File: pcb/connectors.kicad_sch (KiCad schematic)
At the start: 7 parts, among them J1 USB_C_Receptacle_USB2.0, J5 Conn_01x04, U6 USBLC6-2SC6

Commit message: Schematic done, starting PCB design
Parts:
- removed J5: Conn_01x04, Connector_PinSocket_2.54mm:PinSocket_1x04_P2.54mm_Horizontal, symbol Connector_Generic:Conn_01x04
- removed R1, R2, R3, R4: 10.2k, Resistor_SMD:R_0603_1608Metric, symbol Device:R
- added R11 (x4): 10k, Resistor_SMD:R_0603_1608Metric_Pad0.98x0.95mm_HandSolder, symbol Device:R
- added TP1, TP2: TestPoint, TestPoint:TestPoint_Pad_D2.0mm, symbol Connector:TestPoint
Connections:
- net CC1: now also R11.1, R11.1
- net CC2: now also R11.1, R11.1
- net GND: now also R11.2, R11.2, R11.2, R11.2; no longer J1.S1 (SHIELD)
- net SWCLK: now also TP2.1
- net SWDIO: now also TP1.1
- no-connect marks 2 -> 3
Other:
- note added: "Ground loop moment"
- note added: "Solder wires to test points in the unlikely event that you need to debug or enter rescue DP"
- note added: "Try make these 10k resistors toleranced +-5% or lower"
- moved on the sheet: J1, U6

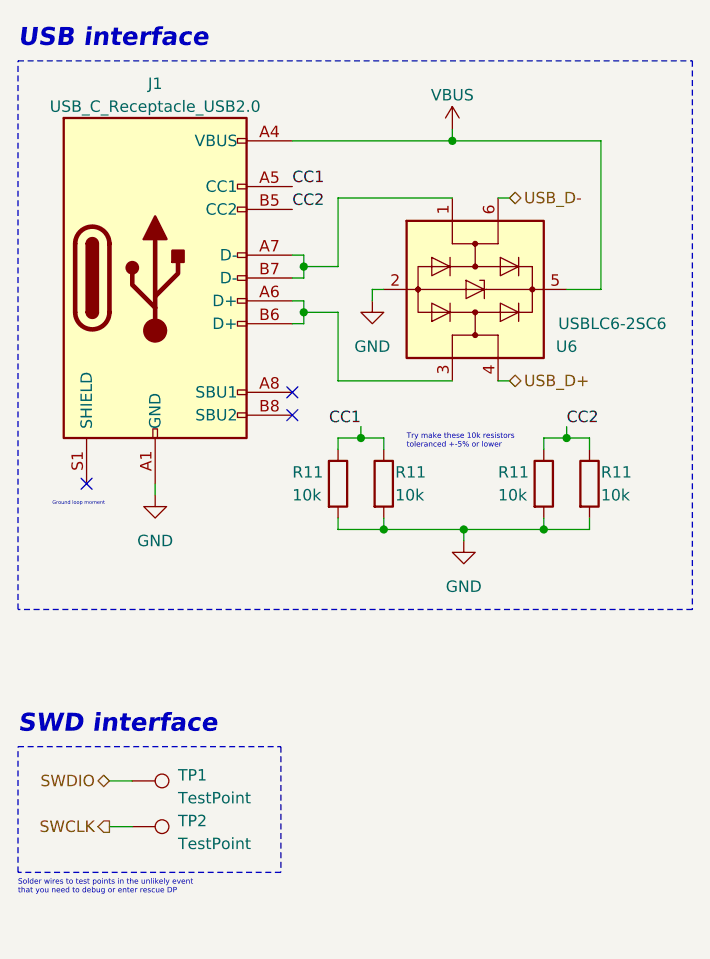
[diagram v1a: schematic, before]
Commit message: Rerouted a lot of stuff
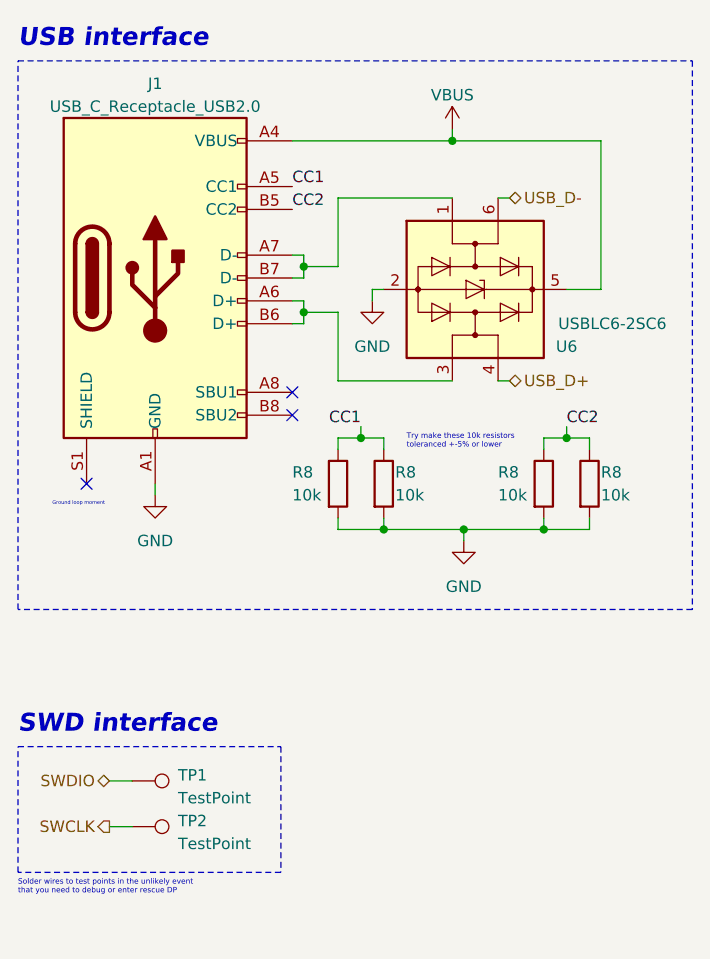
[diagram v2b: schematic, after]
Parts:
- removed R11 (x4): 10k, Resistor_SMD:R_0603_1608Metric_Pad0.98x0.95mm_HandSolder, symbol Device:R
- added R8 (x4): 10k, Resistor_SMD:R_0402_1005Metric, symbol Device:R
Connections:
- net CC1: now also R8.1, R8.1
- net CC2: now also R8.1, R8.1
- net GND: now also R8.2, R8.2, R8.2, R8.2
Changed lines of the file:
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@@
+    )
+  )
+  (symbol (lib_id "Device:R") (at 60.96 72.39 0) (unit 1)
+    (in_bom yes) (on_board yes) (dnp no)
+    (property "Reference" "R8" (at 55.88 71.12 0)
+      (effects (font (size 1.27 1.27)) (justify left))
+    )
+    (property "Value" "10k" (at 55.88 73.66 0)
+      (effects (font (size 1.27 1.27)) (justify left))
+    )
+    (property "Footprint" "Resistor_SMD:R_0402_1005Metric" (at 59.182 72.39 90)
+      (effects (font (size 1.27 1.27)) hide)
+    )
+    (property "Datasheet" "~" (at 60.96 72.39 0)
+      (effects (font (size 1.27 1.27)) hide)
+    )
+    (pin "1")
+    (pin "2")
+    (instances
+      (project "keyboard"
+        (path "/fc529d87-72d0-4c92-b352-ddcf4c6f7199/1c8ac5bd-b3bc-4835-a71b-e635010cd696"
+          (reference "R8") (unit 1)
+        )
+        (path "/fc529d87-72d0-4c92-b352-ddcf4c6f7199/953c467c-8c0d-4158-80e9-7f51ef1515ee"
+          (reference "R7") (unit 1)
+        )
+      )
+    )
+  )
+  (symbol (lib_id "Connector:TestPoint") (at 38.1 110.49 270) (unit 1)
+    (in_bom yes) (on_board yes) (dnp no) (fields_autoplaced)
+    (property "Reference" "TP2" (at 43.18 109.855 90)
+      (effects (font (size 1.27 1.27)) (justify left))
+    )
+    (property "Value" "TestPoint" (at 43.18 112.395 90)
+      (effects (font (size 1.27 1.27)) (justify left))
+    )
+    (property "Footprint" "TestPoint:TestPoint_Pad_D2.0mm" (at 38.1 115.57 0)
+      (effects (font (size 1.27 1.27)) hide)
+    )
+    (property "Datasheet" "~" (at 38.1 115.57 0)
+      (effects (font (size 1.27 1.27)) hide)
+    )
+    (pin "1")
+    (instances
+      (project "keyboard"
+        (path "/fc529d87-72d0-4c92-b352-ddcf4c6f7199/953c467c-8c0d-4158-80e9-7f51ef1515ee"
+          (reference "TP2") (unit 1)
+        )
+      )
     )
   )
   (symbol (lib_id "Device:R") (at 83.82 72.39 0) (unit 1)
     (in_bom yes) (on_board yes) (dnp no)
-    (property "Reference" "R11" (at 78.74 71.12 0)
+    (property "Reference" "R8" (at 78.74 71.12 0)
       (effects (font (size 1.27 1.27)) (justify left))
     )
@@
       (effects (font (size 1.27 1.27)) (justify left))
     )
-    (property "Footprint" "Resistor_SMD:R_0603_1608Metric_Pad0.98x0.95mm_HandSolder" (at 82.042 72.39 90)
+    (property "Footprint" "Resistor_SMD:R_0402_1005Metric" (at 82.042 72.39 90)
       (effects (font (size 1.27 1.27)) hide)
     )
@@
       (project "keyboard"
         (path "/fc529d87-72d0-4c92-b352-ddcf4c6f7199/1c8ac5bd-b3bc-4835-a71b-e635010cd696"
-          (reference "R11") (unit 1)
-        )
-        (path "/fc529d87-72d0-4c92-b352-ddcf4c6f7199/953c467c-8c0d-4158-80e9-7f51ef1515ee"
-          (reference "R6") (unit 1)
-        )
-      )
-    )
-  )
-  (symbol (lib_id "Device:R") (at 66.04 72.39 0) (unit 1)
-    (in_bom yes) (on_board yes) (dnp no)
-    (property "Reference" "R11" (at 67.31 71.12 0)
-      (effects (font (size 1.27 1.27)) (justify left))
-    )
-    (property "Value" "10k" (at 67.31 73.66 0)
-      (effects (font (size 1.27 1.27)) (justify left))
-    )
-    (property "Footprint" "Resistor_SMD:R_0603_1608Metric_Pad0.98x0.95mm_HandSolder" (at 64.262 72.39 90)
-      (effects (font (size 1.27 1.27)) hide)
-    )
-    (property "Datasheet" "~" (at 66.04 72.39 0)
-      (effects (font (size 1.27 1.27)) hide)
-    )
-    (pin "1")
-    (pin "2")
-    (instances
-      (project "keyboard"
-        (path "/fc529d87-72d0-4c92-b352-ddcf4c6f7199/1c8ac5bd-b3bc-4835-a71b-e635010cd696"
-          (reference "R11") (unit 1)
-        )
-        (path "/fc529d87-72d0-4c92-b352-ddcf4c6f7199/953c467c-8c0d-4158-80e9-7f51ef1515ee"
-          (reference "R5") (unit 1)
-        )
-      )
-    )
-  )
-  (symbol (lib_id "Connector:TestPoint") (at 38.1 110.49 270) (unit 1)
-    (in_bom yes) (on_board yes) (dnp no) (fields_autoplaced)
-    (property "Reference" "TP2" (at 43.18 109.855 90)
-      (effects (font (size 1.27 1.27)) (justify left))
-    )
-    (property "Value" "TestPoint" (at 43.18 112.395 90)
-      (effects (font (size 1.27 1.27)) (justify left))
-    )
-    (property "Footprint" "TestPoint:TestPoint_Pad_D2.0mm" (at 38.1 115.57 0)
-      (effects (font (size 1.27 1.27)) hide)
-    )
-    (property "Datasheet" "~" (at 38.1 115.57 0)
-      (effects (font (size 1.27 1.27)) hide)
-    )
-    (pin "1")
-    (instances
-      (project "keyboard"
-        (path "/fc529d87-72d0-4c92-b352-ddcf4c6f7199/953c467c-8c0d-4158-80e9-7f51ef1515ee"
-          (reference "TP2") (unit 1)
+          (reference "R8") (unit 1)
+        )
+        (path "/fc529d87-72d0-4c92-b352-ddcf4c6f7199/953c467c-8c0d-4158-80e9-7f51ef1515ee"
+          (reference "R4") (unit 1)
         )
       )
@@
     )
   )
-  (symbol (lib_id "Device:R") (at 88.9 72.39 0) (unit 1)
-    (in_bom yes) (on_board yes) (dnp no)
-    (property "Reference" "R11" (at 90.17 71.12 0)
-      (effects (font (size 1.27 1.27)) (justify left))
-    )
-    (property "Value" "10k" (at 90.17 73.66 0)
-      (effects (font (size 1.27 1.27)) (justify left))
-    )
-    (property "Footprint" "Resistor_SMD:R_0603_1608Metric_Pad0.98x0.95mm_HandSolder" (at 87.122 72.39 90)
-      (effects (font (size 1.27 1.27)) hide)
-    )
-    (property "Datasheet" "~" (at 88.9 72.39 0)
-      (effects (font (size 1.27 1.27)) hide)
-    )
-    (pin "1")
-    (pin "2")
-    (instances
-      (project "keyboard"
-        (path "/fc529d87-72d0-4c92-b352-ddcf4c6f7199/1c8ac5bd-b3bc-4835-a71b-e635010cd696"
-          (reference "R11") (unit 1)
-        )
-        (path "/fc529d87-72d0-4c92-b352-ddcf4c6f7199/953c467c-8c0d-4158-80e9-7f51ef1515ee"
-          (reference "R7") (unit 1)
+  (symbol (lib_id "Device:R") (at 66.04 72.39 0) (unit 1)
+    (in_bom yes) (on_board yes) (dnp no)
+    (property "Reference" "R8" (at 67.31 71.12 0)
+      (effects (font (size 1.27 1.27)) (justify left))
+    )
+    (property "Value" "10k" (at 67.31 73.66 0)
+      (effects (font (size 1.27 1.27)) (justify left))
+    )
+    (property "Footprint" "Resistor_SMD:R_0402_1005Metric" (at 64.262 72.39 90)
+      (effects (font (size 1.27 1.27)) hide)
+    )
+    (property "Datasheet" "~" (at 66.04 72.39 0)
+      (effects (font (size 1.27 1.27)) hide)
+    )
+    (pin "1")
+    (pin "2")
+    (instances
+      (project "keyboard"
+        (path "/fc529d87-72d0-4c92-b352-ddcf4c6f7199/1c8ac5bd-b3bc-4835-a71b-e635010cd696"
+          (reference "R8") (unit 1)
+        )
+        (path "/fc529d87-72d0-4c92-b352-ddcf4c6f7199/953c467c-8c0d-4158-80e9-7f51ef1515ee"
+          (reference "R6") (unit 1)
         )
       )
@@
     )
   )
-  (symbol (lib_id "Device:R") (at 60.96 72.39 0) (unit 1)
-    (in_bom yes) (on_board yes) (dnp no)
-    (property "Reference" "R11" (at 55.88 71.12 0)
-      (effects (font (size 1.27 1.27)) (justify left))
-    )
-    (property "Value" "10k" (at 55.88 73.66 0)
-      (effects (font (size 1.27 1.27)) (justify left))
-    )
-    (property "Footprint" "Resistor_SMD:R_0603_1608Metric_Pad0.98x0.95mm_HandSolder" (at 59.182 72.39 90)
-      (effects (font (size 1.27 1.27)) hide)
-    )
-    (property "Datasheet" "~" (at 60.96 72.39 0)
-      (effects (font (size 1.27 1.27)) hide)
-    )
-    (pin "1")
-    (pin "2")
-    (instances
-      (project "keyboard"
-        (path "/fc529d87-72d0-4c92-b352-ddcf4c6f7199/1c8ac5bd-b3bc-4835-a71b-e635010cd696"
-          (reference "R11") (unit 1)
-        )
-        (path "/fc529d87-72d0-4c92-b352-ddcf4c6f7199/953c467c-8c0d-4158-80e9-7f51ef1515ee"
-          (reference "R4") (unit 1)
-        )
-      )
+  (symbol (lib_id "Device:R") (at 88.9 72.39 0) (unit 1)
+    (in_bom yes) (on_board yes) (dnp no)
+    (property "Reference" "R8" (at 90.17 71.12 0)
+      (effects (font (size 1.27 1.27)) (justify left))
+    )
+    (property "Value" "10k" (at 90.17 73.66 0)
+      (effects (font (size 1.27 1.27)) (justify left))
+    )
+    (property "Footprint" "Resistor_SMD:R_0402_1005Metric" (at 87.122 72.39 90)
+      (effects (font (size 1.27 1.27)) hide)
+    )
+    (property "Datasheet" "~" (at 88.9 72.39 0)
+      (effects (font (size 1.27 1.27)) hide)
+    )
+    (pin "1")
+    (pin "2")
+    (instances
+      (project "keyboard"
+        (path "/fc529d87-72d0-4c92-b352-ddcf4c6f7199/1c8ac5bd-b3bc-4835-a71b-e635010cd696"
+          (reference "R8") (unit 1)
+        )
+        (path "/fc529d87-72d0-4c92-b352-ddcf4c6f7199/953c467c-8c0d-4158-80e9-7f51ef1515ee"
+          (reference "R5") (unit 1)
+        )
+      )

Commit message: PCB design complete
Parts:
- added TP3: TestPoint, TestPoint:TestPoint_Pad_D2.0mm, symbol Connector:TestPoint
- R8: LCSC (none) -> C25744
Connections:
- net GND: now also TP3.1
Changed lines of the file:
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@@
+    (stroke (width 0) (type default))
+  )
+  (wire (pts (xy 35.56 115.57) (xy 38.1 115.57))
     (stroke (width 0) (type default))
   )
@@
     (fill (type none))
   )
-  (rectangle (start 25.4 101.6) (end 54.61 115.57)
+  (rectangle (start 25.4 101.6) (end 54.61 120.65)
     (stroke (width 0) (type dash))
     (fill (type none))
   )
   (text "Solder wires to test points in the unlikely event\nthat you need to debug or enter rescue DP"
-    (at 25.4 118.11 0)
+    (at 25.4 123.19 0)
     (effects (font (size 0.6 0.6)) (justify left bottom))
   )
@@
   (hierarchical_label "USB_D-" (shape bidirectional) (at 80.01 40.64 0) (fields_autoplaced)
     (effects (font (size 1.27 1.27)) (justify left))
+  )
+  (symbol (lib_id "Connector:TestPoint") (at 38.1 115.57 270) (unit 1)
+    (in_bom yes) (on_board yes) (dnp no) (fields_autoplaced)
+    (property "Reference" "TP3" (at 43.18 114.935 90)
+      (effects (font (size 1.27 1.27)) (justify left))
+    )
+    (property "Value" "TestPoint" (at 43.18 117.475 90)
+      (effects (font (size 1.27 1.27)) (justify left))
+    )
+    (property "Footprint" "TestPoint:TestPoint_Pad_D2.0mm" (at 38.1 120.65 0)
+      (effects (font (size 1.27 1.27)) hide)
+    )
+    (property "Datasheet" "~" (at 38.1 120.65 0)
+      (effects (font (size 1.27 1.27)) hide)
+    )
+    (pin "1")
+    (instances
+      (project "keyboard"
+        (path "/fc529d87-72d0-4c92-b352-ddcf4c6f7199/953c467c-8c0d-4158-80e9-7f51ef1515ee"
+          (reference "TP3") (unit 1)
+        )
+      )
+    )
   )
   (symbol (lib_id "Power_Protection:USBLC6-2SC6") (at 76.2 50.8 270) (unit 1)
@@
       (effects (font (size 1.27 1.27)) hide)
     )
+    (property "LCSC" "C25744" (at 60.96 72.39 0)
+      (effects (font (size 1.27 1.27)) hide)
+    )
     (pin "1")
     (pin "2")
@@
       (effects (font (size 1.27 1.27)) hide)
     )
+    (property "LCSC" "C25744" (at 83.82 72.39 0)
+      (effects (font (size 1.27 1.27)) hide)
+    )
     (pin "1")
     (pin "2")
@@
         (path "/fc529d87-72d0-4c92-b352-ddcf4c6f7199/953c467c-8c0d-4158-80e9-7f51ef1515ee"
           (reference "R4") (unit 1)
+        )
+      )
+    )
+  )
+  (symbol (lib_id "power:GND") (at 35.56 115.57 270) (unit 1)
+    (in_bom yes) (on_board yes) (dnp no) (fields_autoplaced)
+    (property "Reference" "#PWR025" (at 29.21 115.57 0)
+      (effects (font (size 1.27 1.27)) hide)
+    )
+    (property "Value" "GND" (at 31.75 116.205 90)
+      (effects (font (size 1.27 1.27)) (justify right))
+    )
+    (property "Footprint" "" (at 35.56 115.57 0)
+      (effects (font (size 1.27 1.27)) hide)
+    )
+    (property "Datasheet" "" (at 35.56 115.57 0)
+      (effects (font (size 1.27 1.27)) hide)
+    )
+    (pin "1")
+    (instances
+      (project "keyboard"
+        (path "/fc529d87-72d0-4c92-b352-ddcf4c6f7199/953c467c-8c0d-4158-80e9-7f51ef1515ee"
+          (reference "#PWR025") (unit 1)
         )
       )
@@
       (effects (font (size 1.27 1.27)) hide)
     )
+    (property "LCSC" "C25744" (at 66.04 72.39 0)
+      (effects (font (size 1.27 1.27)) hide)
+    )
     (pin "1")
     (pin "2")
@@
       (effects (font (size 1.27 1.27)) hide)
     )
+    (property "LCSC" "C25744" (at 88.9 72.39 0)
+      (effects (font (size 1.27 1.27)) hide)
+    )

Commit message: PCB ready for production
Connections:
- net GND: now also J1.S1 (SHIELD)
- no-connect marks 3 -> 2
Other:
- note removed: "Ground loop moment"
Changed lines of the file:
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@@
   )
   (no_connect (at 55.88 62.23))
-  (no_connect (at 33.02 72.39))
   (no_connect (at 55.88 64.77))
   (wire (pts (xy 55.88 54.61) (xy 57.15 54.61))
@@
   )
   (wire (pts (xy 60.96 40.64) (xy 60.96 48.26))
+    (stroke (width 0) (type default))
+  )
+  (wire (pts (xy 33.02 72.39) (xy 33.02 73.66))
     (stroke (width 0) (type default))
   )
@@
     (at 25.4 123.19 0)
     (effects (font (size 0.6 0.6)) (justify left bottom))
-  )
-  (text "Ground loop moment" (at 29.21 74.93 0)
-    (effects (font (size 0.4 0.4)) (justify left bottom))
   )
   (text "Try make these 10k resistors\ntoleranced +-5% or lower"
@@
         )
       )
+    )
+  )
+  (symbol (lib_id "power:GND") (at 33.02 73.66 0) (unit 1)
+    (in_bom yes) (on_board yes) (dnp no) (fields_autoplaced)
+    (property "Reference" "#PWR026" (at 33.02 80.01 0)
+      (effects (font (size 1.27 1.27)) hide)
+    )
+    (property "Value" "GND" (at 33.02 78.74 0)
+      (effects (font (size 1.27 1.27)))
+    )
+    (property "Footprint" "" (at 33.02 73.66 0)
+      (effects (font (size 1.27 1.27)) hide)
+    )
+    (property "Datasheet" "" (at 33.02 73.66 0)
+      (effects (font (size 1.27 1.27)) hide)
+    )
+    (pin "1")
+    (instances
+      (project "keyboard"
+        (path "/fc529d87-72d0-4c92-b352-ddcf4c6f7199/953c467c-8c0d-4158-80e9-7f51ef1515ee"
+          (reference "#PWR026") (unit 1)
+        )
+      )
